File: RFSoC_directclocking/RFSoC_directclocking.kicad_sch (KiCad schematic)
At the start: 15 parts, among them J1 Conn_Coaxial, J2 Conn_Coaxial, J3 Conn_Coaxial, J4 Conn_Coaxial, J5 Conn_Coaxial, U1 TCM2-33WX+, U2 TCM2-33WX+

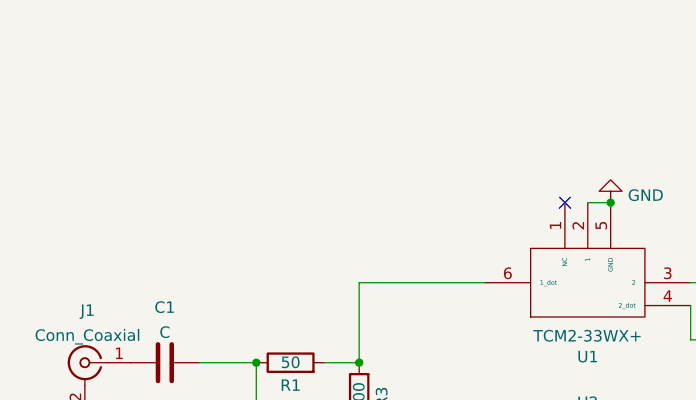
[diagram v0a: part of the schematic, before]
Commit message: pmod board update
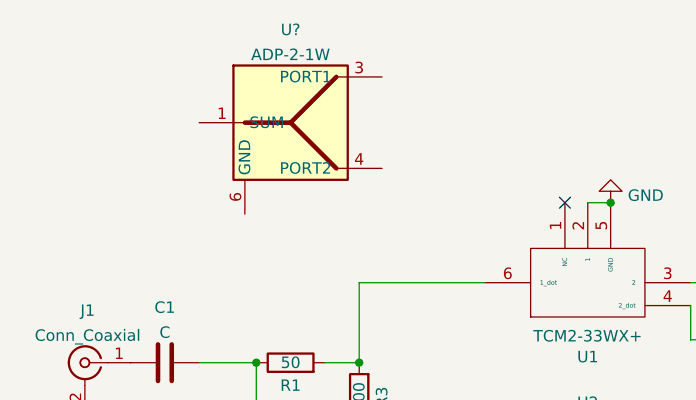
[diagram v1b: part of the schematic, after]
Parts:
- added U?: ADP-2-1W, RF_Mini-Circuits:Mini-Circuits_CD636_LandPatternPL-035, symbol RF:ADP-2-1W
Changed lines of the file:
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@@
     (pin "1")
+  )
+  (symbol (lib_id "RF:ADP-2-1W") (at 114.3 55.88 0) (unit 1)
+    (in_bom yes) (on_board yes) (fields_autoplaced)
+    (property "Reference" "U?" (id 0) (at 114.3 45.5635 0))
+    (property "Value" "ADP-2-1W" (id 1) (at 114.3 48.3386 0))
+    (property "Footprint" "RF_Mini-Circuits:Mini-Circuits_CD636_LandPatternPL-035" (id 2) (at 110.49 67.31 0)
+      (effects (font (size 1.27 1.27)) hide)
+    )
+    (property "Datasheet" "https://www.minicircuits.com/pdfs/ADP-2-1W.pdf" (id 3) (at 113.03 64.77 0)
+      (effects (font (size 1.27 1.27)) hide)
+    )
+    (pin "1")
+    (pin "2")
+    (pin "3")
+    (pin "4")
+    (pin "5")
+    (pin "6")
   )
   (symbol (lib_id "Device:C") (at 167.64 80.01 90) (mirror x) (unit 1)
@@
       (reference "U2") (unit 1) (value "TCM2-33WX+") (footprint "RF_Mini-Circuits:TCM2-33WX+")
     )
+    (path "/d03ca6e0-baba-4066-8996-894335dd1fec"
+      (reference "U?") (unit 1) (value "ADP-2-1W") (footprint "RF_Mini-Circuits:Mini-Circuits_CD636_LandPatternPL-035")
+    )
   )

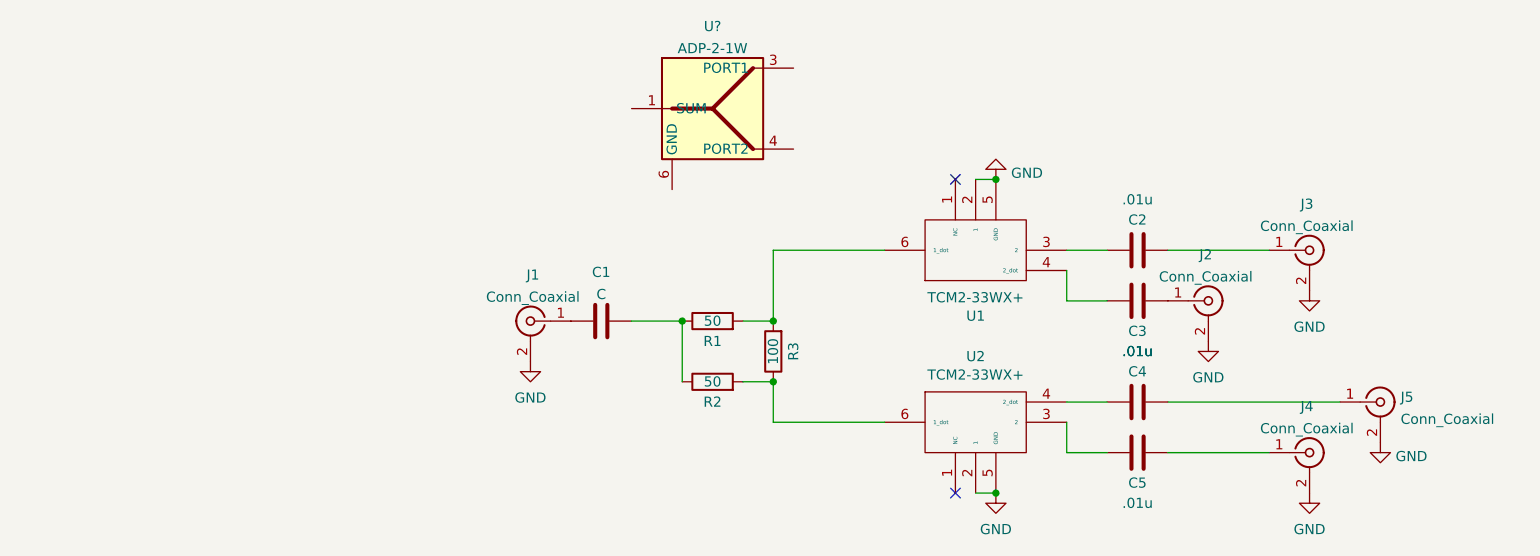
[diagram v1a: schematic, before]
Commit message: Squashed commit of the following:
commit 11c362fd04afcdda8fc54016fc262973d8ee90dd
Author: cody <you@example.com>
Date:   Sat May 14 20:18:42 2022 -0700

    updated silkscreens, degin DRC corrections

commit c03c76887280f84603892cf274eefb7fb13b0fa8
Author: cody <you@example.com>
Date:   Fri May 13 16:10:57 2022 -0700

    fork em

commit e1673cb11a9ebe940ceda00a5b2ec080c415b465
Author: cody <you@example.com>
Date:   Fri May 13 15:38:00 2022 -0700

    updated all

commit 84fbdba19d4f5d8a85804f2c5d387b833a8e7f5e
Author: Cody Roberson <carobers@asu.edu>
Date:   Mon May 9 16:15:14 2022 -0700

    Finished Updated ADC schematic

    ADC schematic was modified to match the pin map between
    the rfsoc and the xm500.

commit 1e4de3bc2e504d4b0d3d294a2c6c5a2a5a485041
Author: cody <you@example.com>
Date:   Mon May 9 10:21:30 2022 -0700

    progress check

    Started Labeling process

commit 6cadb2acb3bb1a794e84b73e4dfc828af985fa6c
Author: cody <you@example.com>
Date:   Thu May 5 15:24:15 2022 -0700

    partial update of labels

commit 2dab10b1dfa9c61606f5d562ab6e543ae0948647
Merge: 76ba8d6 79e9342
Author: Cody Roberson <codyaroberson@outlook.com>
Date:   Wed Mar 9 20:07:10 2022 -0700

    Merge pull request #1 from CodyRoberson/twochannel_clk

    Twochannel clk

commit 79e93425439f23e00c2b0d92e892590d87fe78f7
Author: Cody Roberson <carobers@asu.edu>
Date:   Wed Mar 9 20:04:09 2022 -0700

    moved forkem and labeled ports

commit 9a4b6dc66818e11f3bb9969be501559d1f9e476d
Author: Cody Roberson <carobers@asu.edu>
Date:   Wed Mar 9 16:28:24 2022 -0700

    improvements

    Made improvement to kicad symbol and replaced footprint for baluns. They
    were incorrectly orientated with regards to pin numbering

commit 8d29e46f6a613ffa86cae2f2a7a070122b97e7eb
Author: Cody Roberson <carobers@asu.edu>
Date:   Wed Mar 9 14:50:01 2022 -0700

    added kicad symbol+footprint

commit 3c7e1566d05959f7dad261469b2e27b92f79ed87
Author: Cody Roberson <carobers@asu.edu>
Date:   Wed Mar 9 14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
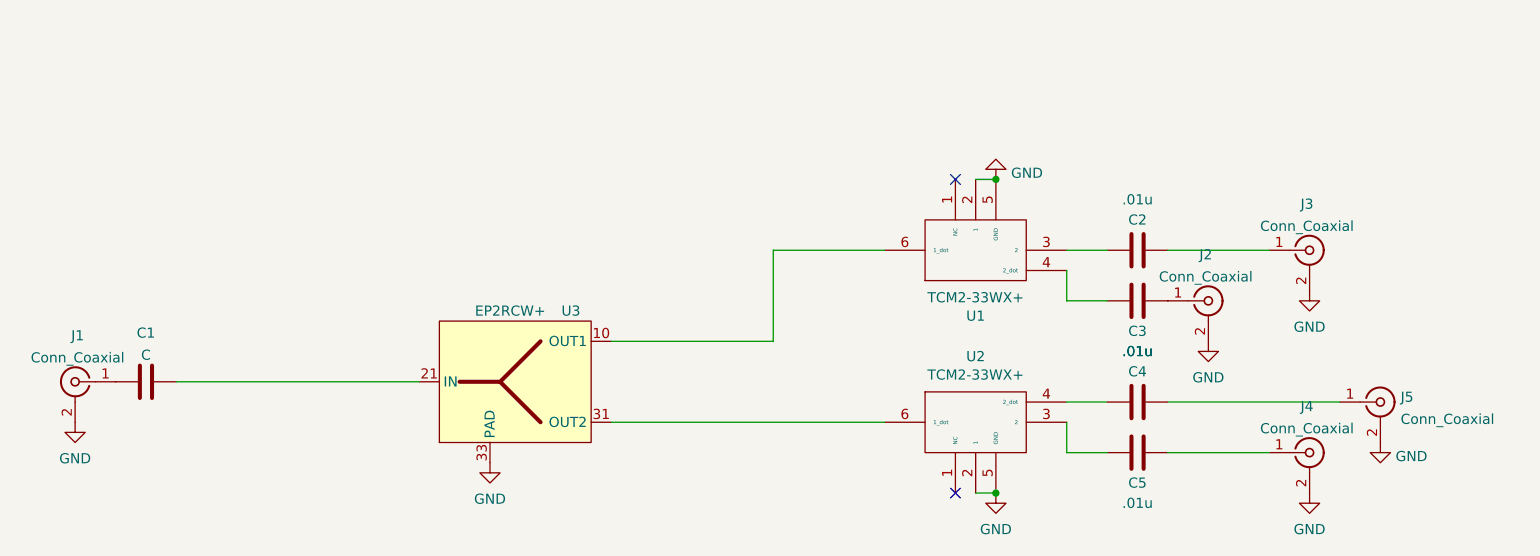
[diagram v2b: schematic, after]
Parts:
- removed R1, R2: 50, Resistor_SMD:R_0402_1005Metric, symbol Device:R
- removed R3: 100, Resistor_SMD:R_0402_1005Metric, symbol Device:R
- removed U?: ADP-2-1W, RF_Mini-Circuits:Mini-Circuits_CD636_LandPatternPL-035, symbol RF:ADP-2-1W
- added U3: EP2RCW+, RF_Mini-Circuits:Mini-Circuits_QQQ130_LandPattern_PL-236_ClockwisePinNumbering, symbol Power Splitter:EP2RCW
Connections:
- net GND: now also U3.1 (NC), U3.11 (GND), U3.12 (NC), U3.13 (NC), U3.14 (NC), U3.15 (NC), U3.16 (NC), U3.17 (NC), U3.18 (NC), U3.19 (NC), U3.2 (NC), U3.20 (GND), U3.22 (GND), U3.23 (NC), U3.24 (NC), U3.25 (NC), U3.26 (NC), U3.27 (NC), U3.28 (NC), U3.29 (NC), U3.3 (NC), U3.30 (GND), U3.32 (GND), U3.33 (PAD), U3.4 (NC), U3.5 (NC), U3.6 (NC), U3.7 (NC), U3.8 (NC), U3.9 (GND)
- net at C1.2: now also U3.21 (IN)
- net at U1.6 (1_dot): now also U3.10 (OUT1)
- net at U2.6 (1_dot): now also U3.31 (OUT2)
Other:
- moved on the sheet: C1, J1
